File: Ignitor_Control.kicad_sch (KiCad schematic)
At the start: 6 parts, among them J13 Screw_Terminal_01x02, K2 PR30-24V-450-1A, Q8 BSS138

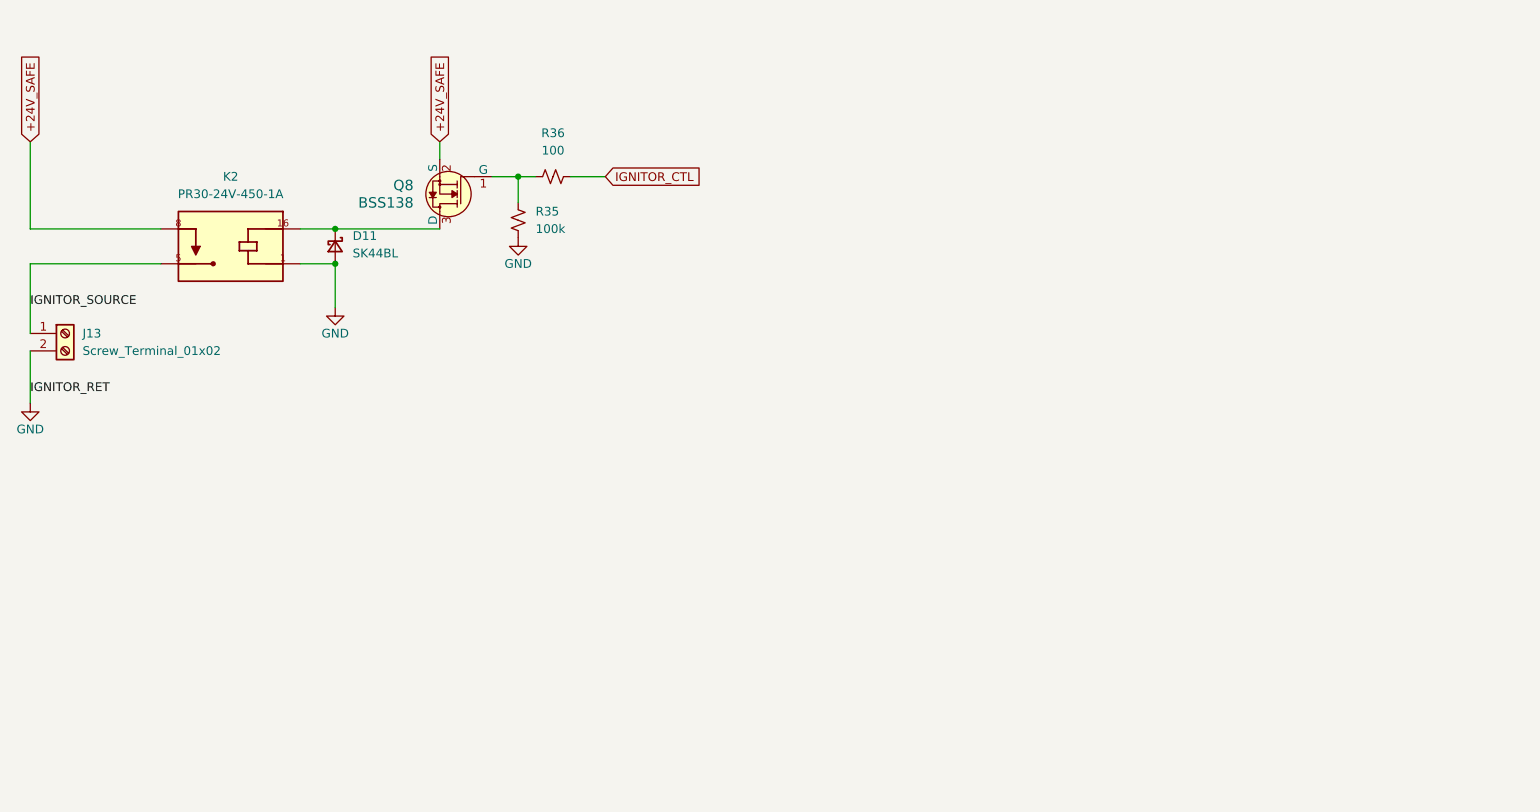
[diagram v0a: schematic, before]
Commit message: Add load cell inputs
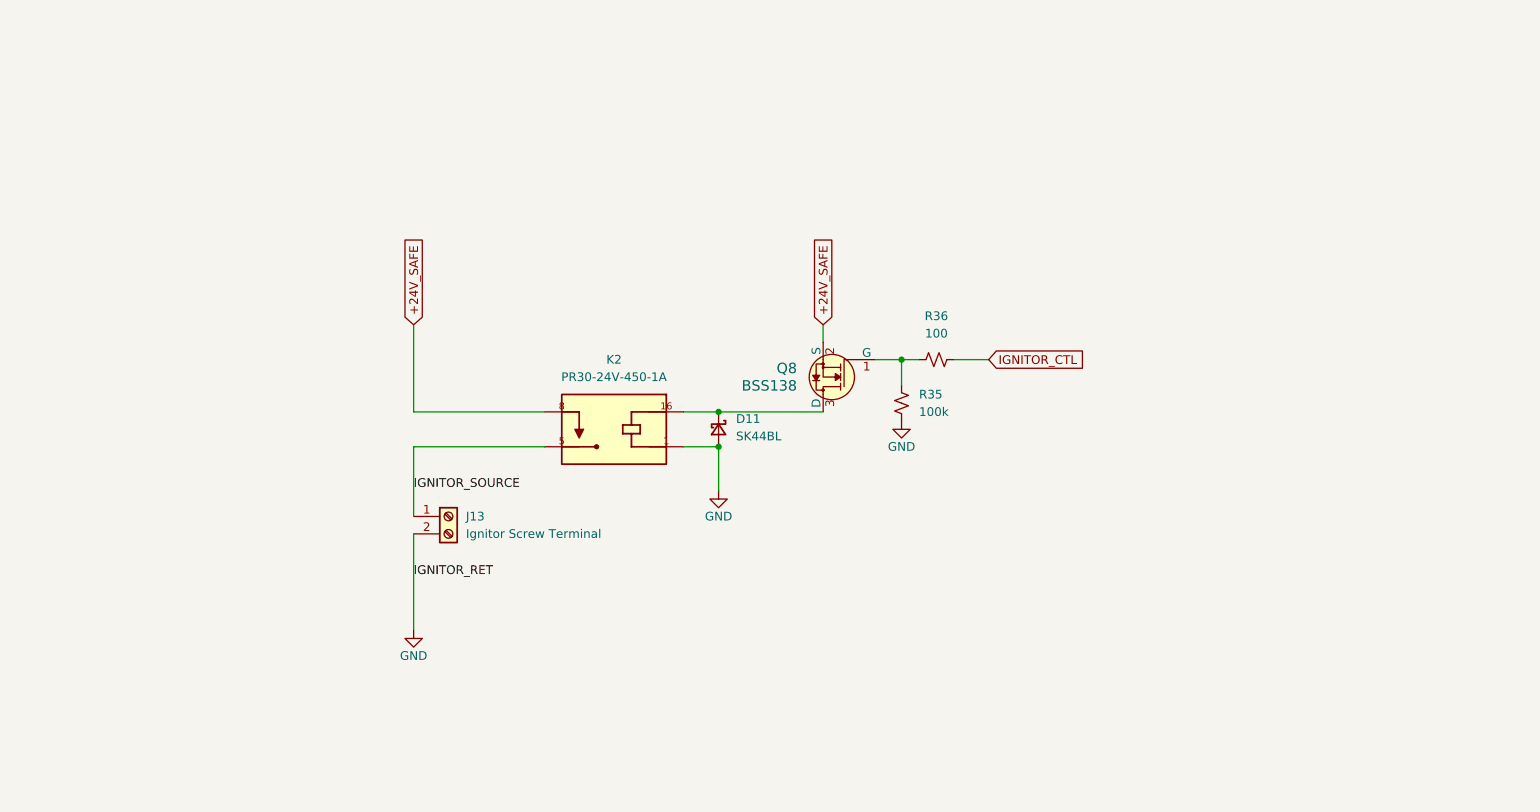
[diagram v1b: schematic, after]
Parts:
- J13: value Screw_Terminal_01x02 -> Ignitor Screw Terminal
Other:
- title: (none) -> Ignitor Control
- moved on the sheet: D11, J13, K2, Q8, R35, R36

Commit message: Add all footprints
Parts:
- removed K2: PR30-24V-450-1A, Solenoid Safeguard:RELAY_PR30-24V-450-1A, symbol PR30-24V-450-1A:PR30-24V-450-1A
- added K3: G5LE-1, Relay_THT:Relay_SPDT_Omron-G5LE-1, symbol Relay:G5LE-1
- R35: value 100k -> 10k; LCSC C25530 -> C25531; MPN 0402WGJ0104TCE -> 0402WGJ0103TCE
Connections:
- net +24V_SAFE: now also K3.1
- net GND: now also K3.5
- net IGNITOR_SOURCE: now also K3.3
- net at D11.1 (K), Q8.3 (D): now also K3.2
- no-connect marks 0 -> 1
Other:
- moved on the sheet: D11, J13, Q8, R36

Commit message: Almost done routing
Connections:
- net IGNITOR_RLY_+VE: now reaches D11.1 (K), K3.2, Q8.3 (D)
- net IGNITOR_CTL_FET: now reaches Q8.1 (G), R35.1, R36.1
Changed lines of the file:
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@@
-	)
-	(junction
-		(at 93.98 83.82)
-		(diameter 0)
-		(color 0 0 0 0)
 	)
 	(junction
@@
 	(wire
 		(pts
-			(xy 161.29 68.58) (xy 161.29 71.12)
+			(xy 161.29 55.88) (xy 161.29 71.12)
 		)
 		(stroke
@@
 	(wire
 		(pts
-			(xy 92.71 83.82) (xy 93.98 83.82)
-		)
-		(stroke
-			(width 0)
-			(type default)
-		)
-	)
-	(wire
-		(pts
-			(xy 180.34 73.66) (xy 185.42 73.66)
+			(xy 180.34 73.66) (xy 199.39 73.66)
 		)
 		(stroke
@@
 			(width 0)
 			(type default)
+		)
+	)
+	(label "IGNITOR_RLY_+VE"
+		(at 135.89 83.82 0)
+		(effects
+			(font
+				(size 1.27 1.27)
+			)
+			(justify left bottom)
 		)
 	)
@@
 		)
 	)
+	(label "IGNITOR_CTL_FET"
+		(at 171.45 73.66 90)
+		(effects
+			(font
+				(size 1.27 1.27)
+			)
+			(justify left bottom)
+		)
+	)
+	(label "+24V_SAFE"
+		(at 161.29 58.42 270)
+		(effects
+			(font
+				(size 1.27 1.27)
+			)
+			(justify right bottom)
+		)
+	)
+	(label "+24V_SAFE"
+		(at 102.87 83.82 0)
+		(effects
+			(font
+				(size 1.27 1.27)
+			)
+			(justify left bottom)
+		)
+	)
+	(label "IGNITOR_CTL_MCU"
+		(at 182.88 73.66 0)
+		(effects
+			(font
+				(size 1.27 1.27)
+			)
+			(justify left bottom)
+		)
+	)
 	(label "IGNITOR_RET"
 		(at 100.33 118.11 0)
@@
 	(global_label "+24V_SAFE"
 		(shape input)
-		(at 161.29 68.58 90)
+		(at 161.29 55.88 90)
 		(fields_autoplaced yes)
 		(effects
@@
 		)
 		(property "Intersheetrefs" "${INTERSHEET_REFS}"
-			(at 161.29 55.0115 90)
+			(at 161.29 42.3115 90)
 			(effects
 				(font
@@
 	(global_label "IGNITOR_CTL"
 		(shape input)
-		(at 185.42 73.66 0)
+		(at 199.39 73.66 0)
 		(fields_autoplaced yes)
 		(effects
@@
 		)
 		(property "Intersheetrefs" "${INTERSHEET_REFS}"
-			(at 200.0167 73.66 0)
+			(at 213.9867 73.66 0)
 			(effects
 				(font

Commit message: routing broken
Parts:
- renumbered D11 to D10, J13 to J21, K3 to K2, R35 to R37, R36 to R38
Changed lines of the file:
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@@
 		(dnp no)
 		(fields_autoplaced yes)
-		(property "Reference" "K3"
+		(property "Reference" "K2"
 			(at 138.43 90.1699 0)
 			(effects
@@
 			(project ""
 				(path "/226c5870-4123-4efa-a2b3-b42d02f59bb7/4e09186f-4067-4c22-bbd5-0048a728fd95"
-					(reference "K3")
+					(reference "K2")
 					(unit 1)
 				)
@@
 		(on_board yes)
 		(dnp no)
-		(property "Reference" "#PWR091"
+		(property "Reference" "#PWR098"
 			(at 100.33 132.08 0)
 			(effects
@@
 			(project "nexus"
 				(path "/226c5870-4123-4efa-a2b3-b42d02f59bb7/4e09186f-4067-4c22-bbd5-0048a728fd95"
-					(reference "#PWR091")
+					(reference "#PWR098")
 					(unit 1)
 				)
@@
 		(on_board yes)
 		(dnp no)
-		(property "Reference" "#PWR089"
+		(property "Reference" "#PWR099"
 			(at 146.05 110.49 0)
 			(effects
@@
 			(project "nexus"
 				(path "/226c5870-4123-4efa-a2b3-b42d02f59bb7/4e09186f-4067-4c22-bbd5-0048a728fd95"
-					(reference "#PWR089")
+					(reference "#PWR099")
 					(unit 1)
 				)
@@
 		(dnp no)
 		(fields_autoplaced yes)
-		(property "Reference" "J13"
+		(property "Reference" "J21"
 			(at 107.95 109.2199 0)
 			(effects
@@
 			(project ""
 				(path "/226c5870-4123-4efa-a2b3-b42d02f59bb7/4e09186f-4067-4c22-bbd5-0048a728fd95"
-					(reference "J13")
+					(reference "J21")
 					(unit 1)
 				)
@@
 		(dnp no)
 		(fields_autoplaced yes)
-		(property "Reference" "R35"
+		(property "Reference" "R37"
 			(at 175.26 78.7399 0)
 			(effects
@@
 			(project "nexus"
 				(path "/226c5870-4123-4efa-a2b3-b42d02f59bb7/4e09186f-4067-4c22-bbd5-0048a728fd95"
-					(reference "R35")
+					(reference "R37")
 					(unit 1)
 				)
@@
 		(dnp no)
 		(fields_autoplaced yes)
-		(property "Reference" "D11"
+		(property "Reference" "D10"
 			(at 157.48 89.9159 90)
 			(effects
@@
 			(project "nexus"
 				(path "/226c5870-4123-4efa-a2b3-b42d02f59bb7/4e09186f-4067-4c22-bbd5-0048a728fd95"
-					(reference "D11")
+					(reference "D10")
 					(unit 1)
 				)
@@
 		(on_board yes)
 		(dnp no)
-		(property "Reference" "#PWR090"
+		(property "Reference" "#PWR0100"
 			(at 172.72 88.9 0)
 			(effects
@@
 			(project "nexus"
 				(path "/226c5870-4123-4efa-a2b3-b42d02f59bb7/4e09186f-4067-4c22-bbd5-0048a728fd95"
-					(reference "#PWR090")
+					(reference "#PWR0100")
 					(unit 1)
 				)
@@
 		(dnp no)
 		(fields_autoplaced yes)
-		(property "Reference" "R36"
+		(property "Reference" "R38"
 			(at 177.8 67.31 90)
 			(effects
@@
 			(project "nexus"
 				(path "/226c5870-4123-4efa-a2b3-b42d02f59bb7/4e09186f-4067-4c22-bbd5-0048a728fd95"
-					(reference "R36")
-					(unit 1)
-				)
+					(reference "R38")
+					(unit 1)
+				)

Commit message: Fix silk screening
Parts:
- J21, K2: now left out of the parts list
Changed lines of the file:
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@@
 	(title_block
 		(title "Ignitor Control")
-		(rev "0.1.0")
+		(rev "1.0.0")
 		(company "Queen's Rocket Engineering Team")
 	)
@@
 		(unit 1)
 		(exclude_from_sim no)
-		(in_bom yes)
+		(in_bom no)
 		(on_board yes)
 		(dnp no)
@@
 		(unit 1)
 		(exclude_from_sim no)
-		(in_bom yes)
+		(in_bom no)
 		(on_board yes)
 		(dnp no)

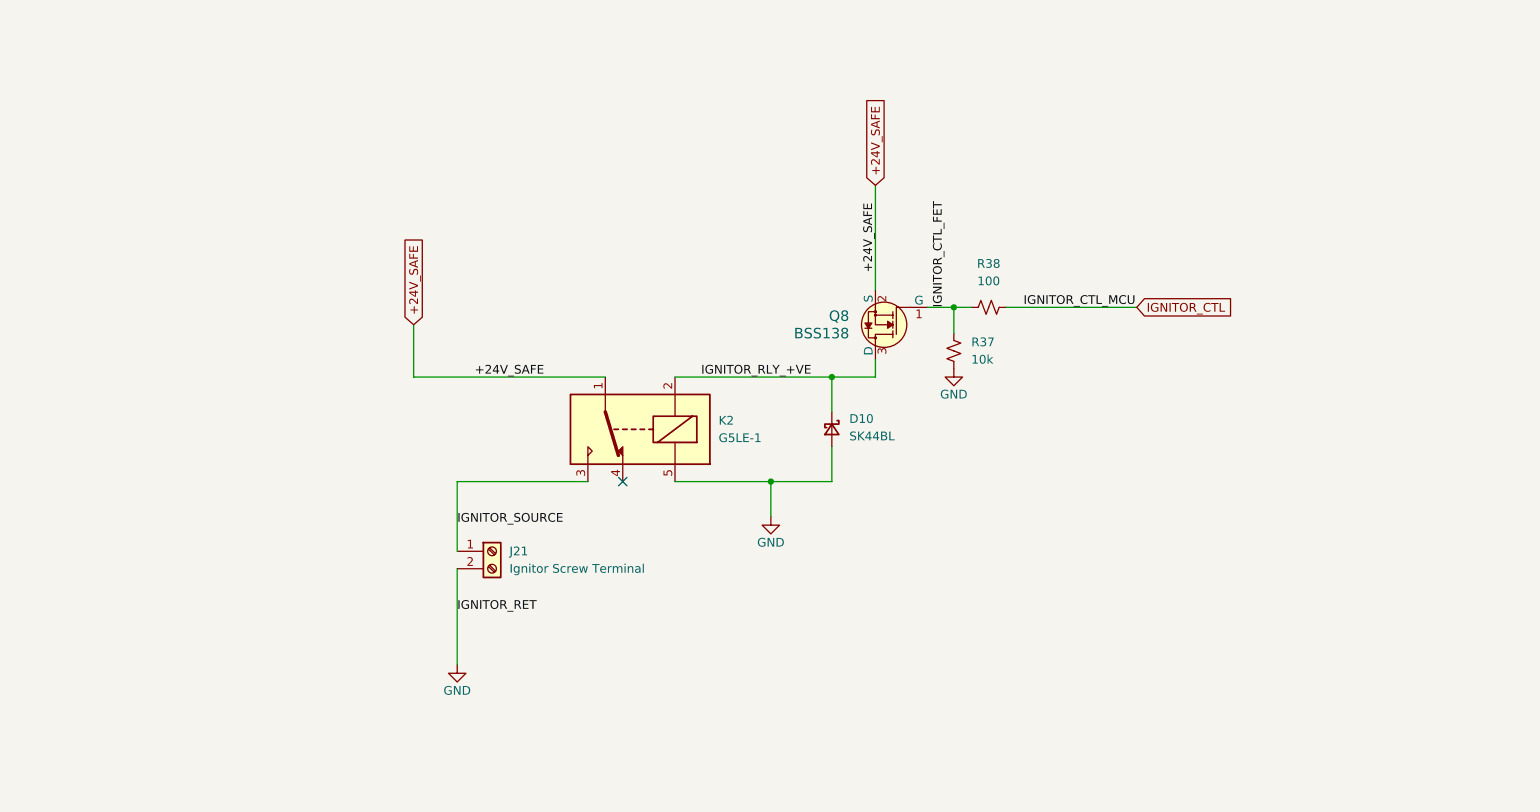
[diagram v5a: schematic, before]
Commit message: Switch relay driving FETs to low side. Relays changed to SPST instead of SPDT
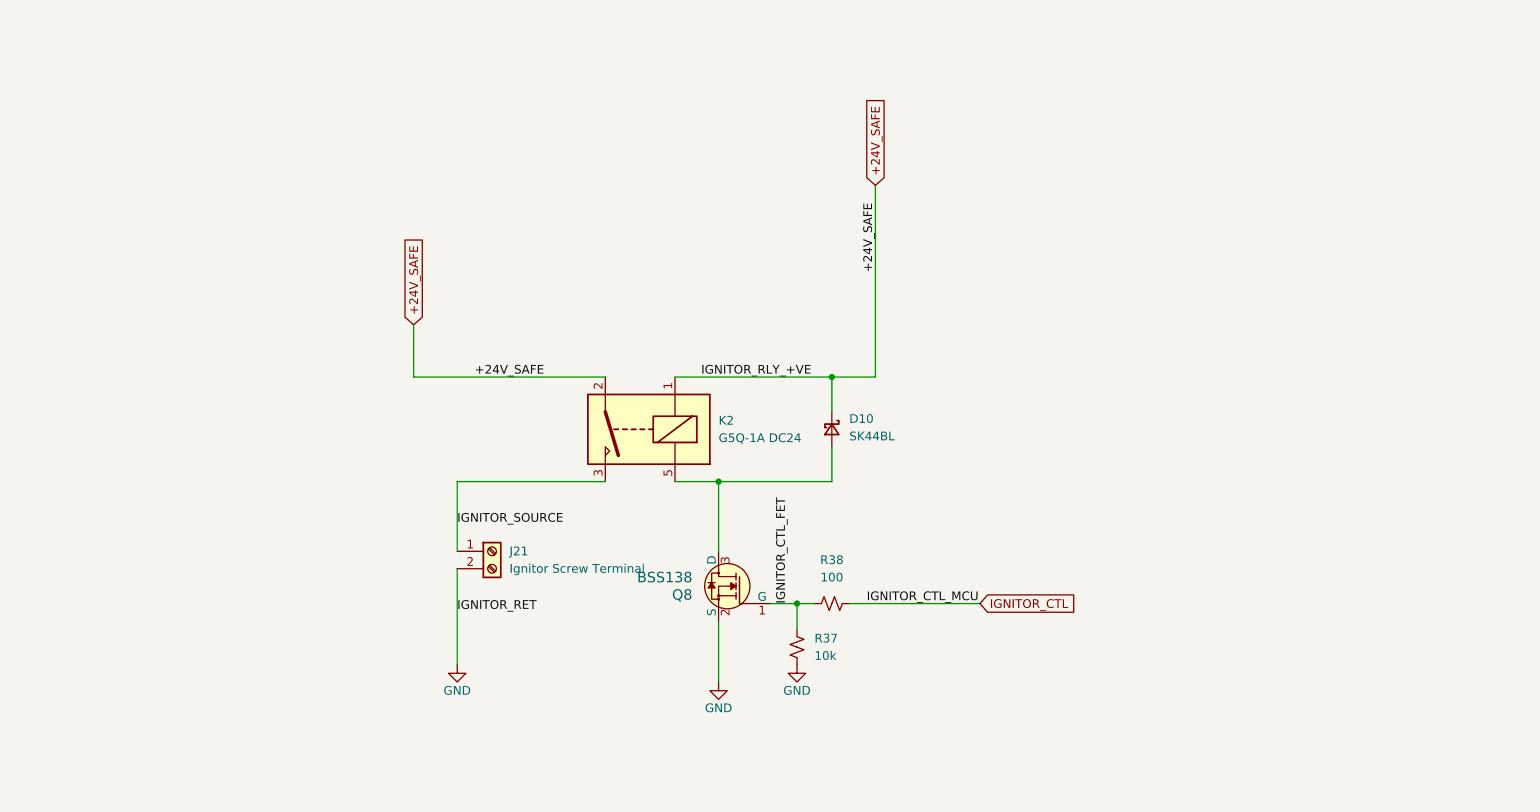
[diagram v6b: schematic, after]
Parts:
- removed K2: G5LE-1, Relay_THT:Relay_SPDT_Omron-G5LE-1, symbol Relay:G5LE-1
- added K2: G5Q-1A DC24, Relay_THT:Relay_SPST_Omron-G5Q-1A, symbol Relay:G5Q-1A
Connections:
- net +24V_SAFE: now also D10.1 (K), K2.1, K2.2; no longer Q8.2 (S)
- net GND: now also Q8.2 (S); no longer D10.2 (A)
- net IGNITOR_SOURCE: now also K2.3
- net IGNITOR_RLY_+VE: no longer names the net of Q8.3 (D)
- net IGNITOR_RLY_+VE: now also D10.2 (A), K2.5; no longer D10.1 (K)
- no-connect marks 1 -> 0
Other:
- moved on the sheet: Q8, R37, R38

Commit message: Add current sensing and fuse mount for IGN
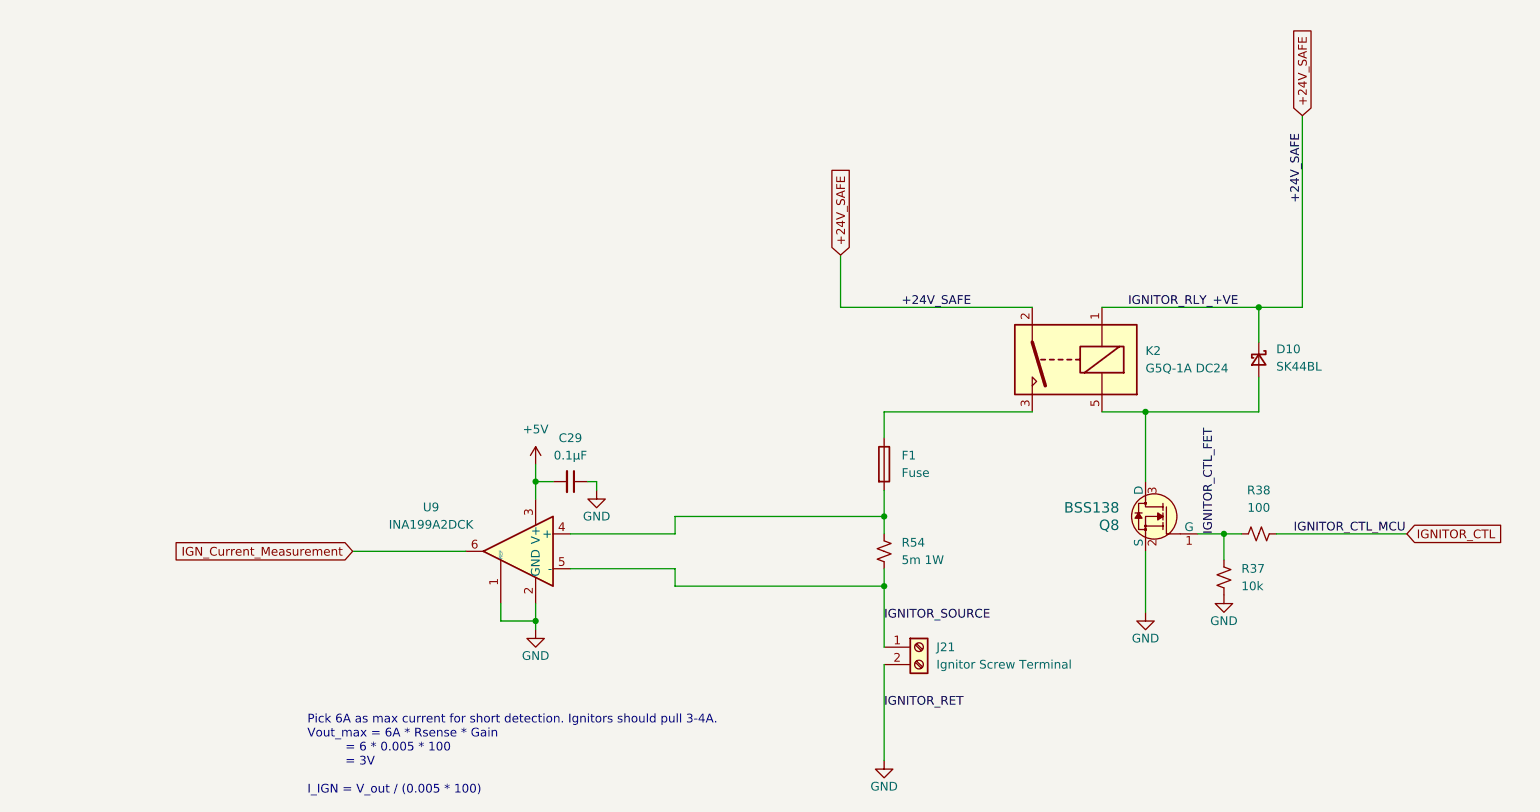
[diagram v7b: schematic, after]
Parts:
- added C29: 0.1μF, Capacitor_SMD:C_0402_1005Metric, symbol Device:C_Small
- added F1: Fuse, Fuse:Fuseholder_Blade_Mini_Keystone_3568, symbol Device:Fuse
- added R54: 5m 1W, Resistor_SMD:R_1206_3216Metric, symbol Device:R_Small_US
- added U9: INA199A2DCK, Package_TO_SOT_SMD:SOT-363_SC-70-6, symbol Amplifier_Current:INA199xxDCK
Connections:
- net GND: now also C29.1, U9.1 (REF), U9.2 (GND)
- net IGNITOR_SOURCE: now also R54.2, U9.5 (-); no longer K2.3
- new net: F1.2, R54.1, U9.4 (+)
- new net: F1.1, K2.3
- new net +5V: C29.2, U9.3 (V+)
- new net IGN_Current_Measurement: U9.6
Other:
- note added: "Pick 6A as max current for short detection. Ignitors should pull 3-4A. Vout_max = 6A * Rsense * Gain = 6 * 0.005 * 100 = 3V I_IGN = V_out / (0.005 * 100)"
- moved on the sheet: D10, J21, K2, Q8, R37, R38

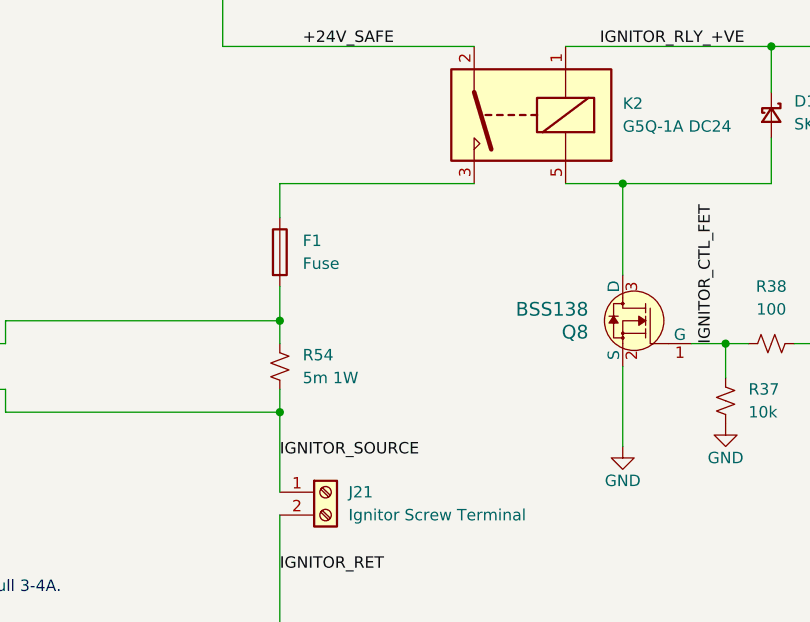
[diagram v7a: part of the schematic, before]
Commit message: Add indicator LEDs and digital +24VSafe detection line
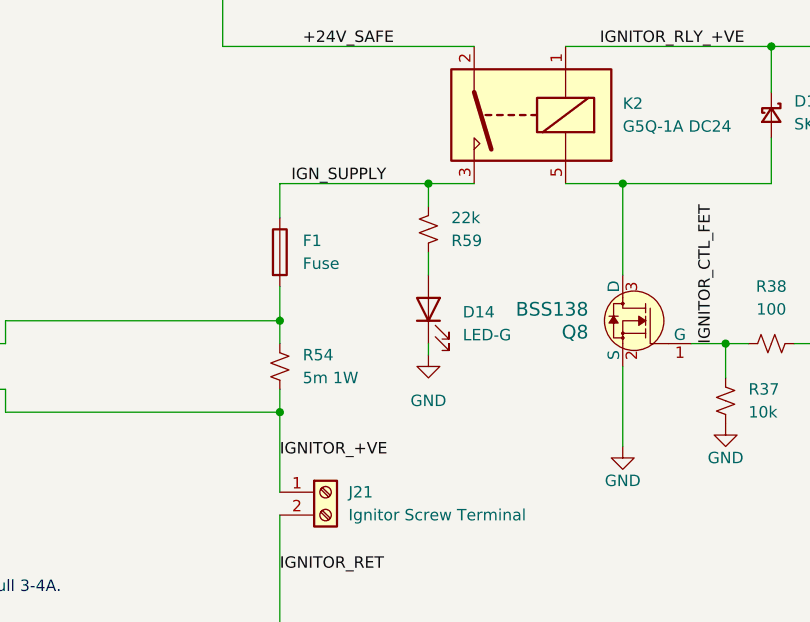
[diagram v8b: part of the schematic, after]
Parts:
- added D14: LED-G, LED_SMD:LED_0805_2012Metric, symbol Device:LED
- added R59: 22k, Resistor_SMD:R_0402_1005Metric, symbol Device:R_Small_US
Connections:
- net GND: now also D14.1 (K)
- net IGN_SUPPLY: now reaches F1.1, K2.3
- net IGN_SUPPLY: now also R59.2
- net IGNITOR_SOURCE renamed IGNITOR_+VE
- new net: D14.2 (A), R59.1
